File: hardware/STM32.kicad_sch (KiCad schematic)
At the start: 17 parts

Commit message: Primeiro protótipo da PCB
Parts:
- C110, C111, C112, C113, C114, C116: footprint (none) -> Capacitor_SMD:C_0603_1608Metric_Pad1.08x0.95mm_HandSolder
- C115: value (none) -> 100n; footprint (none) -> Capacitor_SMD:C_0603_1608Metric_Pad1.08x0.95mm_HandSolder
- D105, D106: footprint (none) -> LED_SMD:LED_0805_2012Metric_Pad1.15x1.40mm_HandSolder
- R119, R120, R121, R123: value (none) -> 10k; footprint (none) -> Resistor_SMD:R_0603_1608Metric_Pad0.98x0.95mm_HandSolder
- R122: value (none) -> BOOT0; footprint (none) -> Jumper:SolderJumper-2_P1.3mm_Open_RoundedPad1.0x1.5mm
- R301: value (none) -> JUMP0; footprint (none) -> Jumper:SolderJumper-2_P1.3mm_Open_RoundedPad1.0x1.5mm
- R302: footprint (none) -> Resistor_SMD:R_0603_1608Metric_Pad0.98x0.95mm_HandSolder
- U301: value (none) -> STM32F103C8Tx; footprint (none) -> Package_QFP:LQFP-48_7x7mm_P0.5mm
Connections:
- net ADC1_IN0: now also U301.14 (PA4); no longer U301.10 (PA0)
- net ADC1_IN1: now also U301.13 (PA3); no longer U301.11 (PA1)
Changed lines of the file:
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@@
   (no_connect (at 166.37 143.51))
   (no_connect (at 166.37 107.95))
+  (no_connect (at 133.35 105.41))
   (no_connect (at 166.37 97.79))
   (no_connect (at 166.37 123.19))
@@
   (no_connect (at 133.35 120.65))
   (no_connect (at 166.37 90.17))
-  (no_connect (at 133.35 110.49))
   (no_connect (at 166.37 130.81))
   (no_connect (at 166.37 100.33))
   (no_connect (at 133.35 118.11))
   (no_connect (at 133.35 133.35))
+  (no_connect (at 133.35 107.95))
+  (no_connect (at 133.35 110.49))
   (no_connect (at 166.37 87.63))
   (no_connect (at 166.37 118.11))
@@
   (no_connect (at 133.35 135.89))
   (no_connect (at 166.37 115.57))
-  (no_connect (at 133.35 115.57))
-  (no_connect (at 133.35 113.03))
   (no_connect (at 166.37 95.25))
   (no_connect (at 166.37 120.65))
@@
     (stroke (width 0) (type default) (color 0 0 0 0))
   )
-  (wire (pts (xy 114.3 107.95) (xy 133.35 107.95))
+  (wire (pts (xy 114.3 113.03) (xy 133.35 113.03))
     (stroke (width 0) (type default) (color 0 0 0 0))
   )
@@
     (stroke (width 0) (type default) (color 0 0 0 0))
   )
-  (wire (pts (xy 114.3 105.41) (xy 133.35 105.41))
+  (wire (pts (xy 114.3 115.57) (xy 133.35 115.57))
     (stroke (width 0) (type default) (color 0 0 0 0))
   )
@@
     (effects (font (size 1.27 1.27)) (justify left))
   )
-  (hierarchical_label "ADC1_IN0" (shape input) (at 114.3 105.41 180)
+  (hierarchical_label "ADC1_IN0" (shape input) (at 114.3 115.57 180)
     (effects (font (size 1.27 1.27)) (justify right))
   )
@@
     (effects (font (size 1.27 1.27)) (justify left))
   )
-  (hierarchical_label "ADC1_IN1" (shape input) (at 114.3 107.95 180)
+  (hierarchical_label "ADC1_IN1" (shape input) (at 114.3 113.03 180)
     (effects (font (size 1.27 1.27)) (justify right))
   )
@@
     (in_bom yes) (on_board yes)
     (property "Reference" "C115" (id 0) (at 110.49 77.47 90))
-    (property "Value" "" (id 1) (at 110.49 67.31 90))
-    (property "Footprint" "" (id 2) (at 111.76 72.39 0)
+    (property "Value" "100n" (id 1) (at 110.49 67.31 90))
+    (property "Footprint" "Capacitor_SMD:C_0603_1608Metric_Pad1.08x0.95mm_HandSolder" (id 2) (at 111.76 72.39 0)
       (effects (font (size 1.27 1.27)) hide)
     )
@@
       (effects (font (size 1.27 1.27)) (justify right))
     )
-    (property "Footprint" "" (id 2) (at 214.63 116.84 90)
+    (property "Footprint" "LED_SMD:LED_0805_2012Metric_Pad1.15x1.40mm_HandSolder" (id 2) (at 214.63 116.84 90)
       (effects (font (size 1.27 1.27)) hide)
     )
@@
       (effects (font (size 1.27 1.27)) (justify bottom))
     )
-    (property "Value" "" (id 1) (at 212.09 114.3 90)
+    (property "Value" "10k" (id 1) (at 212.09 114.3 90)
       (effects (font (size 1.27 1.27)) (justify bottom))
     )
-    (property "Footprint" "" (id 2) (at 212.09 109.22 0)
+    (property "Footprint" "Resistor_SMD:R_0603_1608Metric_Pad0.98x0.95mm_HandSolder" (id 2) (at 212.09 109.22 0)
       (effects (font (size 1.27 1.27)) hide)
     )
@@
     (in_bom yes) (on_board yes)
     (property "Reference" "R120" (id 0) (at 212.09 101.7016 90))
-    (property "Value" "" (id 1) (at 212.09 104.013 90))
-    (property "Footprint" "" (id 2) (at 212.09 106.68 0)
+    (property "Value" "10k" (id 1) (at 212.09 104.013 90))
+    (property "Footprint" "Resistor_SMD:R_0603_1608Metric_Pad0.98x0.95mm_HandSolder" (id 2) (at 212.09 106.68 0)
       (effects (font (size 1.27 1.27)) hide)
     )
@@
       (effects (font (size 1.27 1.27)) (justify right))
     )
-    (property "Footprint" "" (id 2) (at 222.25 116.84 90)
+    (property "Footprint" "LED_SMD:LED_0805_2012Metric_Pad1.15x1.40mm_HandSolder" (id 2) (at 222.25 116.84 90)
       (effects (font (size 1.27 1.27)) hide)
     )
@@
       (effects (font (size 1.27 1.27)) (justify right))
     )
-    (property "Value" "" (id 1) (at 255.0414 84.963 0)
+    (property "Value" "10k" (id 1) (at 255.0414 84.963 0)
       (effects (font (size 1.27 1.27)) (justify right))
     )
-    (property "Footprint" "" (id 2) (at 256.54 83.82 0)
+    (property "Footprint" "Resistor_SMD:R_0603_1608Metric_Pad0.98x0.95mm_HandSolder" (id 2) (at 256.54 83.82 0)
       (effects (font (size 1.27 1.27)) hide)
     )
@@
     (in_bom yes) (on_board yes)
     (property "Reference" "R123" (id 0) (at 223.4184 90.17 90))
-    (property "Value" "" (id 1) (at 221.107 90.17 90))
-    (property "Footprint" "" (id 2) (at 218.44 90.17 0)
+    (property "Value" "10k" (id 1) (at 221.107 90.17 90))
+    (property "Footprint" "Resistor_SMD:R_0603_1608Metric_Pad0.98x0.95mm_HandSolder" (id 2) (at 218.44 90.17 0)
       (effects (font (size 1.27 1.27)) hide)
     )
@@
     (in_bom yes) (on_board yes)
     (property "Reference" "R122" (id 0) (at 223.52 83.82 90))
-    (property "Value" "" (id 1) (at 220.98 83.82 90))
-    (property "Footprint" "" (id 2) (at 218.44 85.09 0)
+    (property "Value" "BOOT0" (id 1) (at 220.98 83.82 90))
+    (property "Footprint" "Jumper:SolderJumper-2_P1.3mm_Open_RoundedPad1.0x1.5mm" (id 2) (at 218.44 85.09 0)
       (effects (font (size 1.27 1.27)) hide)
     )
@@
     (property "Reference" "C111" (id 0) (at 100.33 77.47 90))
     (property "Value" "100n" (id 1) (at 100.33 67.31 90))
-    (property "Footprint" "" (id 2) (at 101.6 72.39 0)
+    (property "Footprint" "Capacitor_SMD:C_0603_1608Metric_Pad1.08x0.95mm_HandSolder" (id 2) (at 101.6 72.39 0)
       (effects (font (size 1.27 1.27)) hide)
     )
@@
     (property "Reference" "C114" (id 0) (at 107.95 77.47 90))
     (property "Value" "100n" (id 1) (at 107.95 67.31 90))
-    (property "Footprint" "" (id 2) (at 109.22 72.39 0)
+    (property "Footprint" "Capacitor_SMD:C_0603_1608Metric_Pad1.08x0.95mm_HandSolder" (id 2) (at 109.22 72.39 0)
       (effects (font (size 1.27 1.27)) hide)
     )
@@
       (effects (font (size 1.27 1.27)) hide)
     )
-    (property "Value" "" (id 1) (at 218.44 76.4342 0))
+    (property "Value" "+3.3V" (id 1) (at 218.44 76.4342 0))
     (property "Footprint" "" (id 2) (at 218.44 80.01 0)
       (effects (font (size 1.27 1.27)) hide)
@@
     (property "Reference" "C113" (id 0) (at 105.41 77.47 90))
     (property "Value" "100n" (id 1) (at 105.41 67.31 90))
-    (property "Footprint" "" (id 2) (at 106.68 72.39 0)
+    (property "Footprint" "Capacitor_SMD:C_0603_1608Metric_Pad1.08x0.95mm_HandSolder" (id 2) (at 106.68 72.39 0)
       (effects (font (size 1.27 1.27)) hide)
     )
@@
     (property "Reference" "C112" (id 0) (at 102.87 77.47 90))
     (property "Value" "100n" (id 1) (at 102.87 67.31 90))
-    (property "Footprint" "" (id 2) (at 104.14 72.39 0)
+    (property "Footprint" "Capacitor_SMD:C_0603_1608Metric_Pad1.08x0.95mm_HandSolder" (id 2) (at 104.14 72.39 0)
       (effects (font (size 1.27 1.27)) hide)
     )
@@
     (property "Reference" "C116" (id 0) (at 252.73 90.17 90))
     (property "Value" "100n" (id 1) (at 257.81 86.36 90))
-    (property "Footprint" "" (id 2) (at 256.54 91.44 0)
+    (property "Footprint" "Capacitor_SMD:C_0603_1608Metric_Pad1.08x0.95mm_HandSolder" (id 2) (at 256.54 91.44 0)
       (effects (font (size 1.27 1.27)) hide)
     )
@@
     (property "Reference" "C110" (id 0) (at 87.63 63.5 90))
     (property "Value" "100n" (id 1) (at 87.63 53.34 90))
-    (property "Footprint" "" (id 2) (at 88.9 58.42 0)
+    (property "Footprint" "Capacitor_SMD:C_0603_1608Metric_Pad1.08x0.95mm_HandSolder" (id 2) (at 88.9 58.42 0)
       (effects (font (size 1.27 1.27)) hide)
     )
@@
       (effects (font (size 1.27 1.27)) hide)
     )
-    (property "Value" "" (id 1) (at 95.25 47.2242 0))
+    (property "Value" "+3.3V" (id 1) (at 95.25 47.2242 0))
     (property "Footprint" "" (id 2) (at 95.25 50.8 0)
       (effects (font (size 1.27 1.27)) hide)
@@
       (effects (font (size 1.27 1.27)) (justify right))
     )
-    (property "Value" "" (id 1) (at 156.4387 150.6173 0)
+    (property "Value" "STM32F103C8Tx" (id 1) (at 156.4387 150.6173 0)
       (effects (font (size 1.27 1.27)) (justify right))
     )
-    (property "Footprint" "" (id 2) (at 163.83 146.05 0)
+    (property "Footprint" "Package_QFP:LQFP-48_7x7mm_P0.5mm" (id 2) (at 163.83 146.05 0)
       (effects (font (size 1.27 1.27)) (justify right) hide)
     )
@@
     (property "Reference" "R302" (id 0) (at 223.4184 143.51 90))
     (property "Value" "10k" (id 1) (at 221.107 143.51 90))
-    (property "Footprint" "" (id 2) (at 218.44 143.51 0)
+    (property "Footprint" "Resistor_SMD:R_0603_1608Metric_Pad0.98x0.95mm_HandSolder" (id 2) (at 218.44 143.51 0)
       (effects (font (size 1.27 1.27)) hide)
     )
@@
     (in_bom yes) (on_board yes)
     (property "Reference" "R301" (id 0) (at 223.52 137.16 90))
-    (property "Value" "" (id 1) (at 220.98 137.16 90))
-    (property "Footprint" "" (id 2) (at 218.44 138.43 0)
-      (effects (font (size 1.27 1.27)) hide)
-    )
+    (property "Value" "JUMP0" (id 1) (at 220.98 137.16 90))
+    (property "Footprint" "Jumper:SolderJumper-2_P1.3mm_Open_RoundedPad1.0x1.5mm" (id 2) (at 218.44 138.43 0)
+      (effects (font (size 1.27 1.27)) hide)
+    )

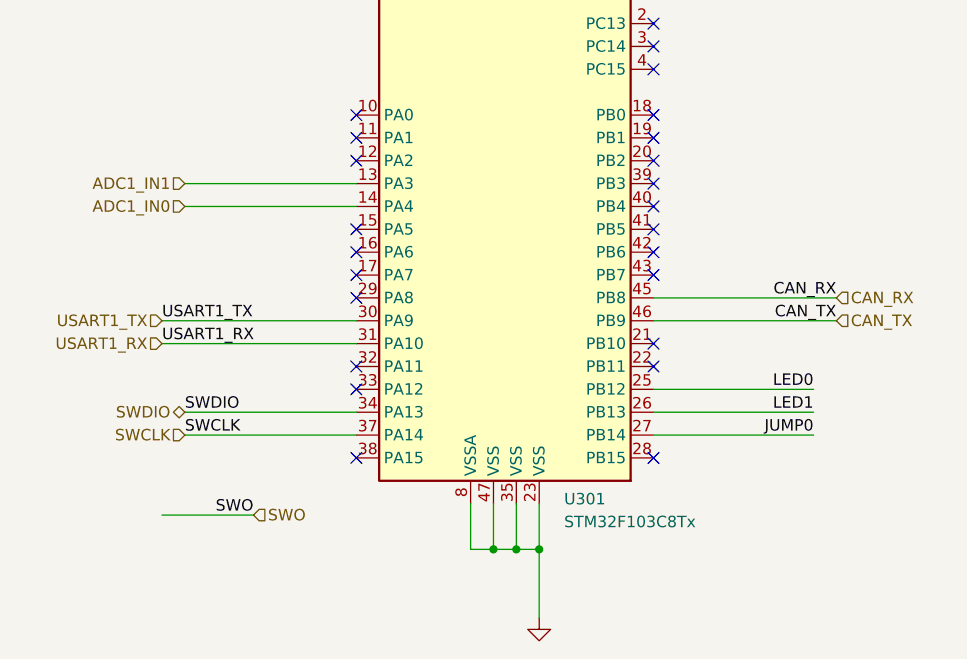
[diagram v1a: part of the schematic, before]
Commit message: hardware: STM32, PCB design in progress
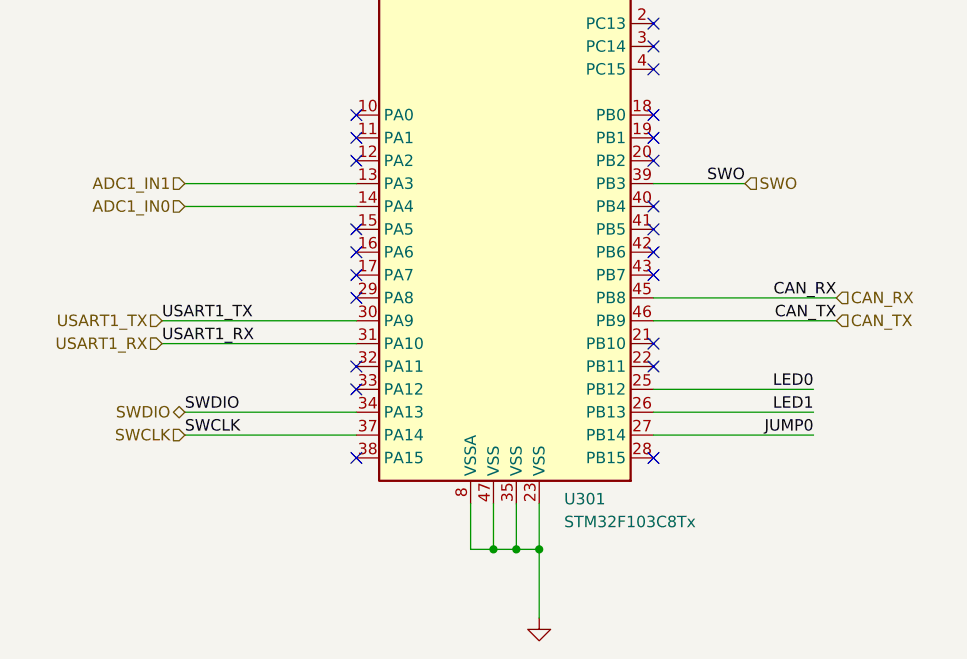
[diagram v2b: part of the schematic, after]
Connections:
- net SWO: now also U301.39 (PB3)
- no-connect marks 26 -> 25
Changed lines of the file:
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@@
   (no_connect (at 166.37 123.19))
   (no_connect (at 133.35 123.19))
-  (no_connect (at 133.35 120.65))
   (no_connect (at 166.37 90.17))
   (no_connect (at 166.37 130.81))
@@
   (no_connect (at 166.37 133.35))
   (no_connect (at 133.35 135.89))
+  (no_connect (at 133.35 120.65))
   (no_connect (at 166.37 115.57))
   (no_connect (at 166.37 95.25))
@@
   (no_connect (at 166.37 110.49))
   (no_connect (at 166.37 105.41))
-  (no_connect (at 166.37 113.03))
   (wire (pts (xy 203.2 140.97) (xy 218.44 140.97))
     (stroke (width 0) (type default) (color 0 0 0 0))
@@
     (stroke (width 0) (type default) (color 0 0 0 0))
   )
-  (wire (pts (xy 121.92 149.86) (xy 111.76 149.86))
+  (wire (pts (xy 176.53 113.03) (xy 166.37 113.03))
     (stroke (width 0) (type default) (color 0 0 0 0))
   )
@@
     (effects (font (size 1.27 1.27)) (justify left bottom))
   )
-  (label "SWO" (at 121.92 149.86 180)
+  (label "SWO" (at 176.53 113.03 180)
     (effects (font (size 1.27 1.27)) (justify right bottom))
   )
@@
     (effects (font (size 1.27 1.27)) (justify left bottom))
   )
-  (hierarchical_label "SWO" (shape input) (at 121.92 149.86 0)
+  (hierarchical_label "SWO" (shape input) (at 176.53 113.03 0)
     (effects (font (size 1.27 1.27)) (justify left))
   )
